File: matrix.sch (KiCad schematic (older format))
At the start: 133 parts

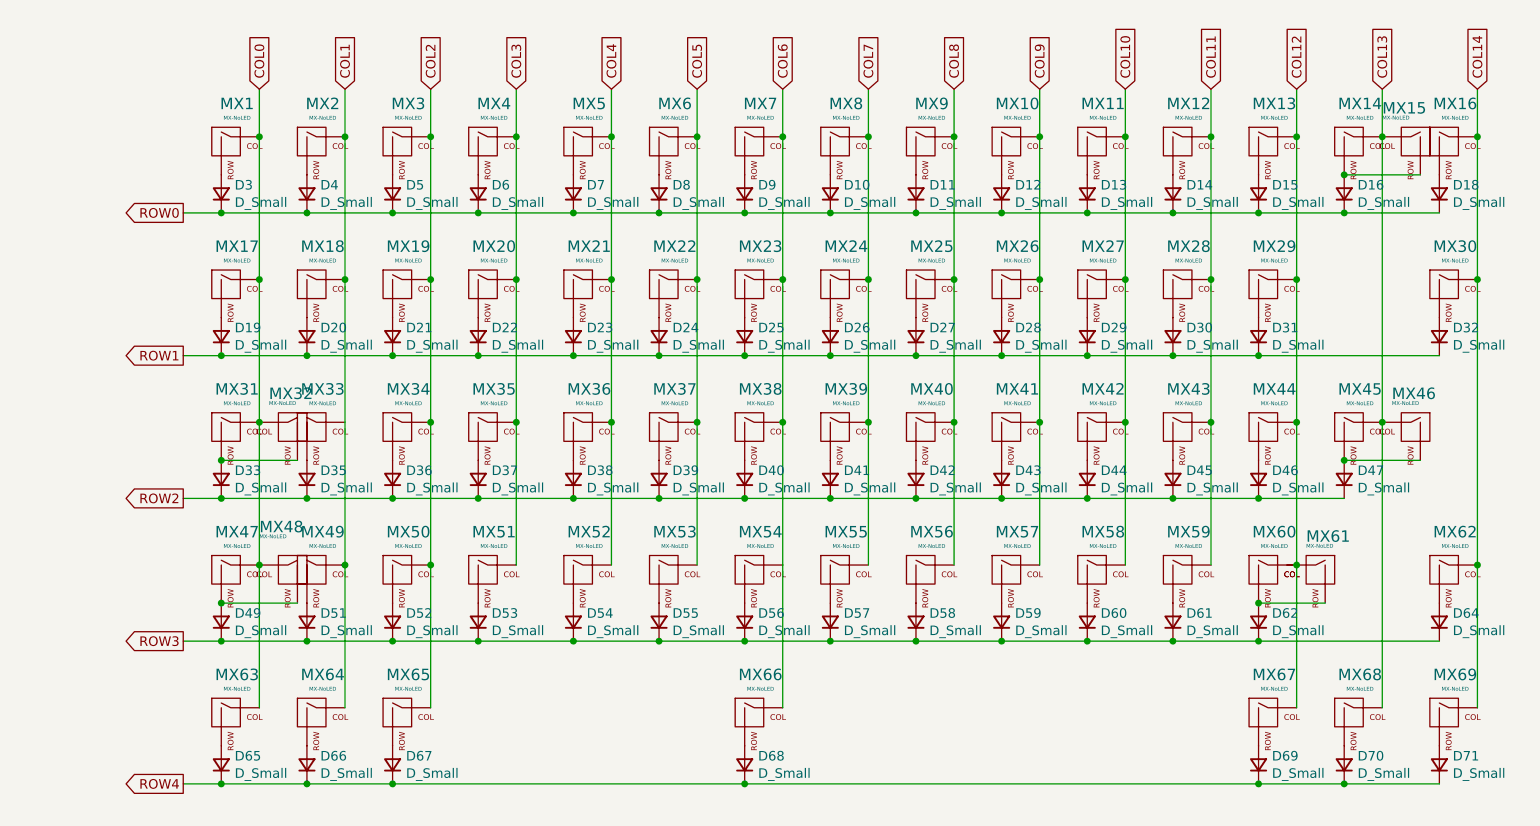
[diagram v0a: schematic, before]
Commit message: fixed schematic flaws and caps lock (thanks Martin!)
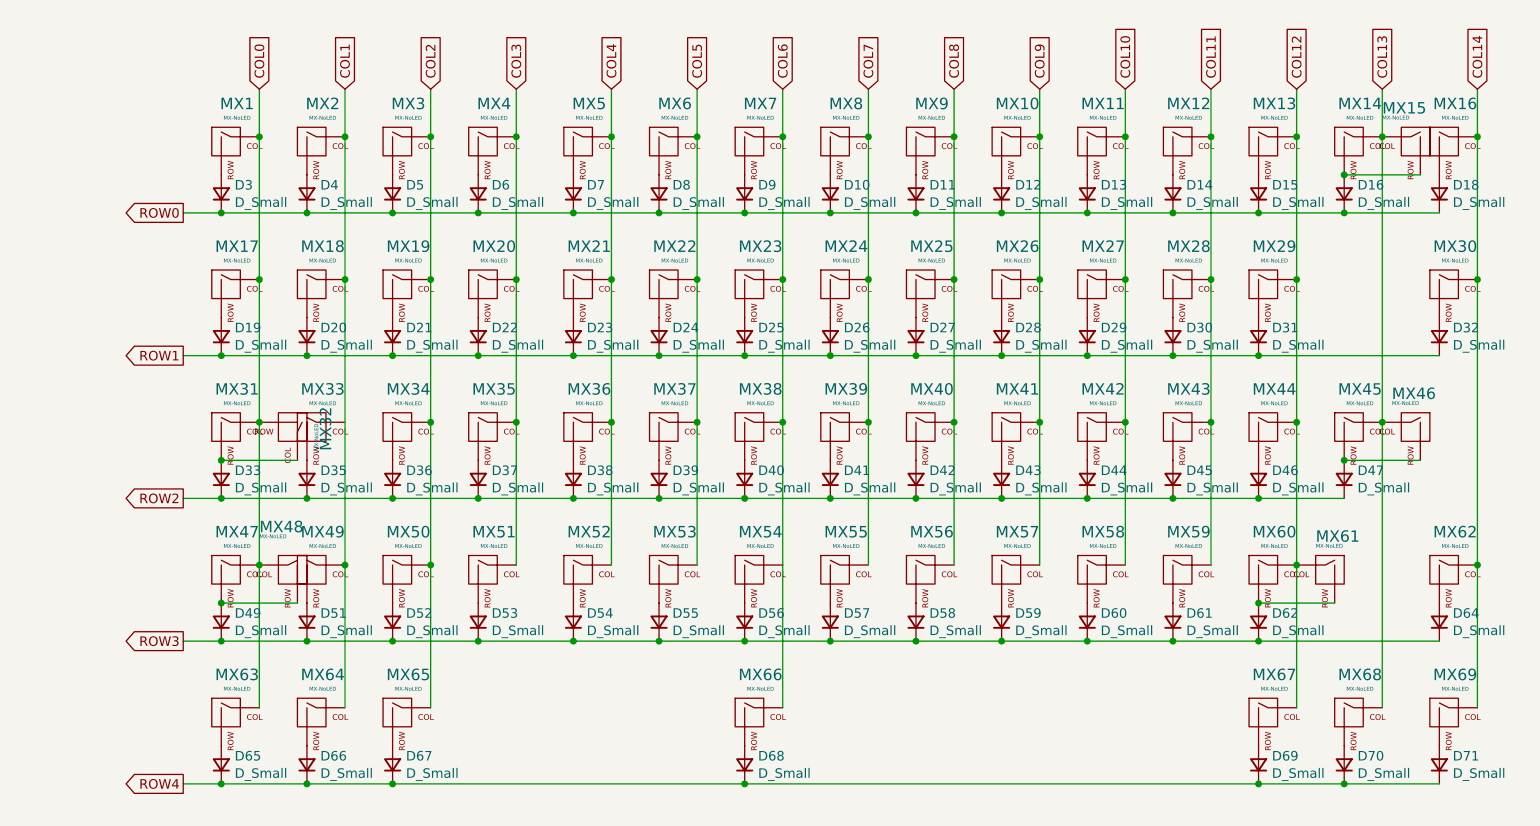
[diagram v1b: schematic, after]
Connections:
- net COL0: now also MX32.2 (ROW); no longer MX32.1 (COL)
- net COL12: now also MX61.1 (COL)
- net at D33.2 (A), MX31.2 (ROW): now also MX32.1 (COL); no longer MX32.2 (ROW)
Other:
- moved on the sheet: MX61
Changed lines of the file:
@@
 	7300 2100 7300 2850
 Connection ~ 7300 2100
-Wire Wire Line
-	7300 3600 7300 4350
 $Comp
 L MX_Alps_Hybrid:MX-NoLED MX16
@@
 Connection ~ 7300 3600
 Connection ~ 7300 2850
-$Comp
-L MX_Alps_Hybrid:MX-NoLED MX61
-U 1 1 61165F70
-P 7400 3650
-F 0 "MX61" H 7450 3850 60  0000 R CNN
-F 1 "MX-NoLED" H 7450 3800 20  0000 R CNN
-F 2 "MX_Only:MXOnly-2.75U-NoLED" H 6775 3625 60  0001 C CNN
-F 3 "" H 6775 3625 60  0001 C CNN
-	1    7400 3650
-	-1   0    0    -1
-$EndComp
 Connection ~ 7100 4000
 $Comp
@@
 F 3 "" H 1375 2875 60  0001 C CNN
 	1    2000 2900
-	-1   0    0    -1
+	0    1    1    0
 $EndComp
 Wire Wire Line
@@
 	2050 3800 1650 3800
 Connection ~ 1650 3800
-Wire Wire Line
-	2050 3050 1650 3050
 Connection ~ 1650 3050
 Wire Wire Line
@@
 Wire Wire Line
 	7100 4000 8050 4000
-Wire Wire Line
-	7450 3800 7100 3800
 Connection ~ 7100 3800
 Wire Wire Line
@@
 Connection ~ 2100 3250
 Connection ~ 1650 3250
+Wire Wire Line
+	7300 3600 7300 4350
+$Comp
+L MX_Alps_Hybrid:MX-NoLED MX61
+U 1 1 61165F70
+P 7450 3650
+F 0 "MX61" H 7500 3850 60  0000 R CNN
+F 1 "MX-NoLED" H 7500 3800 20  0000 R CNN
+F 2 "MX_Only:MXOnly-2.75U-NoLED" H 6825 3625 60  0001 C CNN
+F 3 "" H 6825 3625 60  0001 C CNN
+	1    7450 3650
+	-1   0    0    -1
+$EndComp
+Wire Wire Line
+	7100 3800 7500 3800
+Wire Wire Line
+	1650 3050 2050 3050
 $EndSCHEMATC

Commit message: minor fixes
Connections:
- net COL1: now also MX33.1 (COL)
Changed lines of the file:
@@
 	-1   0    0    -1
 $EndComp
-Wire Wire Line
-	2300 3600 2300 2100
-Connection ~ 2300 3600
 Connection ~ 2300 1350
 Wire Wire Line
@@
 	2750 1350 2750 2100
 Connection ~ 2100 2500
-Connection ~ 2300 2100
 Wire Wire Line
 	2300 2100 2300 1350
@@
 Wire Wire Line
 	1650 3050 2050 3050
+Wire Wire Line
+	2300 3600 2300 2850
+Connection ~ 2300 3600
+Wire Wire Line
+	2300 2850 2300 2100
+Connection ~ 2300 2850
+Connection ~ 2300 2100
 $EndSCHEMATC

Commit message: updated branch and ordered pcb prototype
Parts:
- D10, D11, D12, D13, D14, D15, D16, D18, D19, D20, D21, D22, D23, D24, D25, D26, D27, D28, D29, D3, D30, D31, D32, D33, D35, D36, D37, D38, D39, D4, D40, D41, D42, D43, D44, D45, D46, D47, D49, D5, D51, D52, D53, D54, D55, D56, D57, D58, D59, D6, D60, D61, D62, D64, D65, D66, D67, D68, D69, D7, D70, D71, D8, D9: value D_Small -> 1n4148; footprint Diode_SMD:D_0603_1608Metric -> Diode_SMD:D_SOD-323F; JLCPCB (none) -> C2128

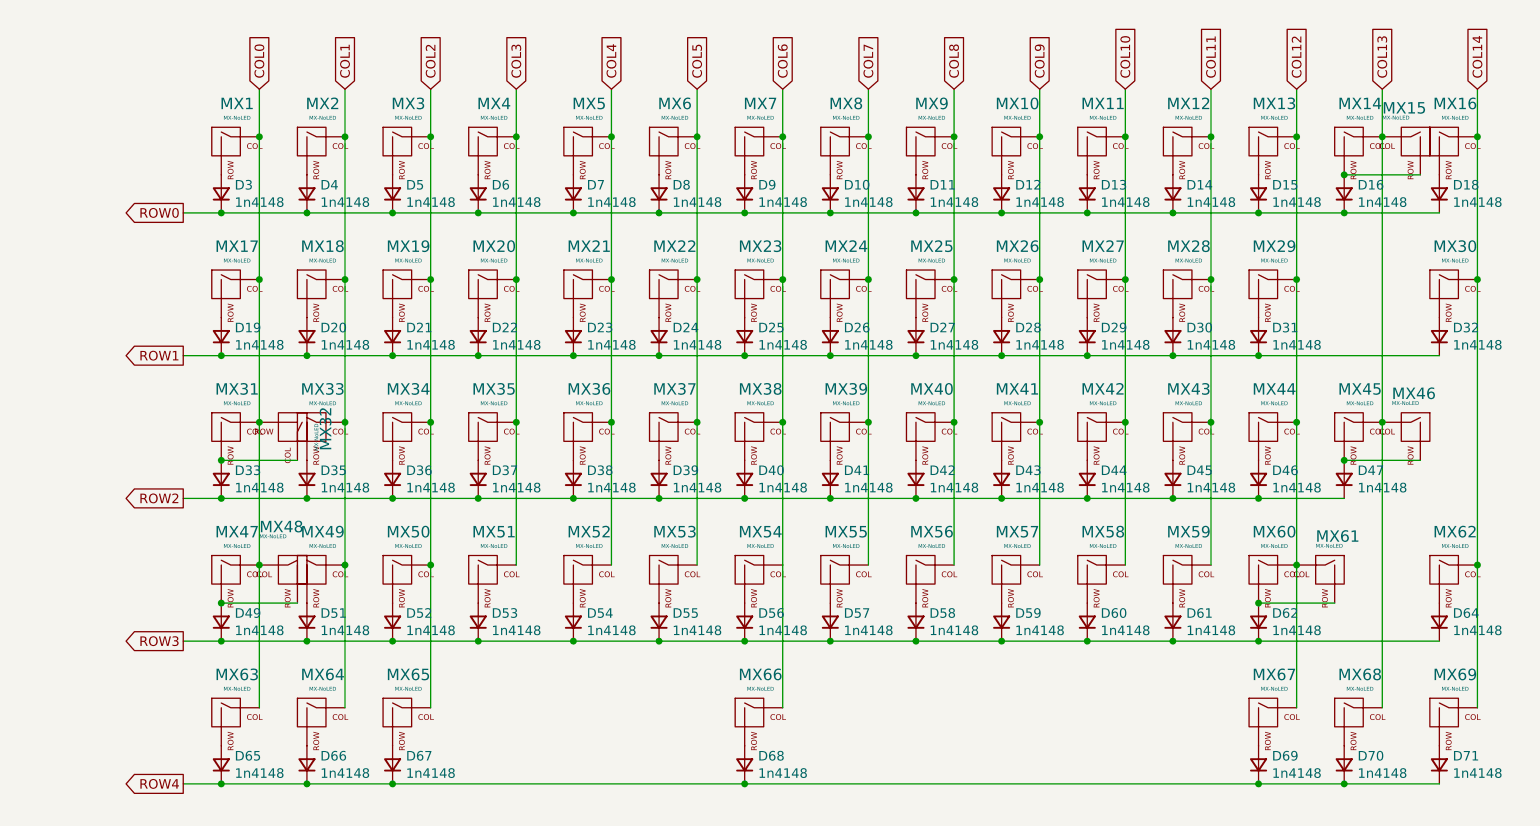
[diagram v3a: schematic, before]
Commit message: modified to use BAV70 diodes
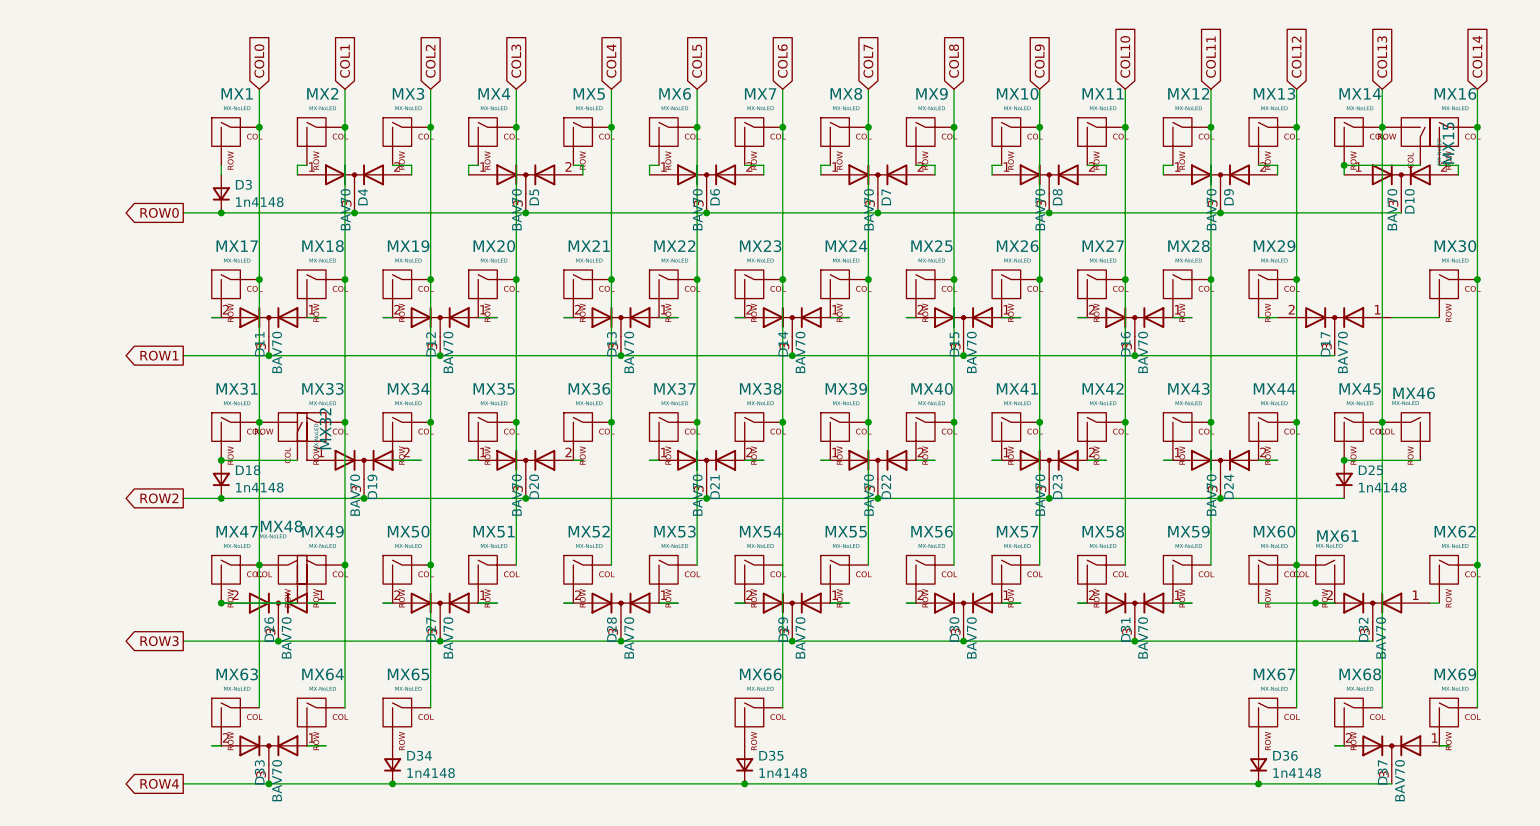
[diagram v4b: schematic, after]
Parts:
- removed D10, D11, D12, D13, D14, D15, D16, D18, D19, D20, D21, D22, D23, D24, D25, D26, D27, D28, D29, D30, D31, D32, D35, D36, D37, D38, D39, D4, D40, D41, D42, D43, D44, D45, D46, D49, D5, D51, D52, D53, D54, D55, D56, D57, D58, D59, D6, D60, D61, D62, D64, D65, D66, D7, D70, D71, D8, D9: 1n4148, Diode_SMD:D_SOD-323F, symbol Device:D_Small
- added D10, D11, D12, D13, D14, D15, D16, D17, D19, D20, D21, D22, D23, D24, D26, D27, D28, D29, D30, D31, D32, D33, D37, D4, D5, D6, D7, D8, D9: BAV70, Package_TO_SOT_SMD:SOT-23, symbol Diode:BAV70
- renumbered D33 to D18, D47 to D25, D67 to D34, D68 to D35, D69 to D36
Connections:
- net COL13: now also MX15.2 (ROW); no longer MX15.1 (COL)
- net ROW0: now also D10.3 (K), D4.3 (K), D5.3 (K), D6.3 (K), D7.3 (K), D8.3 (K), D9.3 (K)
- net ROW1: now also D11.3 (K), D12.3 (K), D13.3 (K), D14.3 (K), D15.3 (K), D16.3 (K), D17.3 (K)
- net ROW2: now also D19.3 (K), D20.3 (K), D21.3 (K), D22.3 (K), D23.3 (K), D24.3 (K)
- net ROW3: now also D26.3 (K), D27.3 (K), D28.3 (K), D29.3 (K), D30.3 (K), D31.3 (K), D32.3 (K)
- net ROW4: now also D33.3 (K), D37.3 (K)
- net at MX2.2 (ROW): now also D4.1 (A)
- net at MX17.2 (ROW): now also D11.2 (A)
- net at MX47.2 (ROW), MX48.2 (ROW): now also D26.2 (A)
- net at MX49.2 (ROW): now also D26.1 (A)
- net at MX63.2 (ROW): now also D33.2 (A)
- net at MX64.2 (ROW): now also D33.1 (A)
- net at MX3.2 (ROW): now also D4.2 (A)
- net at MX4.2 (ROW): now also D5.1 (A)
- net at MX18.2 (ROW): now also D11.1 (A)
- net at MX19.2 (ROW): now also D12.2 (A)
- net at MX34.2 (ROW): now also D19.2 (A)
- net at MX35.2 (ROW): now also D20.1 (A)
- net at MX50.2 (ROW): now also D27.2 (A)
- net at MX51.2 (ROW): now also D27.1 (A)
- net at MX5.2 (ROW): now also D5.2 (A)
- net at MX6.2 (ROW): now also D6.1 (A)
- net at MX21.2 (ROW): now also D13.2 (A)
- net at MX22.2 (ROW): now also D13.1 (A)
- net at MX36.2 (ROW): now also D20.2 (A)
- net at MX37.2 (ROW): now also D21.1 (A)
- net at MX52.2 (ROW): now also D28.2 (A)
- net at MX53.2 (ROW): now also D28.1 (A)
- net at MX7.2 (ROW): now also D6.2 (A)
- net at MX8.2 (ROW): now also D7.1 (A)
- net at MX23.2 (ROW): now also D14.2 (A)
- net at MX24.2 (ROW): now also D14.1 (A)
- net at MX38.2 (ROW): now also D21.2 (A)
- net at MX39.2 (ROW): now also D22.1 (A)
- net at MX54.2 (ROW): now also D29.2 (A)
- net at MX55.2 (ROW): now also D29.1 (A)
- net at MX9.2 (ROW): now also D7.2 (A)
- net at MX10.2 (ROW): now also D8.1 (A)
- net at MX25.2 (ROW): now also D15.2 (A)
- net at MX26.2 (ROW): now also D15.1 (A)
- net at MX40.2 (ROW): now also D22.2 (A)
- net at MX41.2 (ROW): now also D23.1 (A)
- net at MX56.2 (ROW): now also D30.2 (A)
- net at MX57.2 (ROW): now also D30.1 (A)
- net at MX11.2 (ROW): now also D8.2 (A)
- net at MX12.2 (ROW): now also D9.1 (A)
- net at MX27.2 (ROW): now also D16.2 (A)
- net at MX28.2 (ROW): now also D16.1 (A)
- net at MX42.2 (ROW): now also D23.2 (A)
- net at MX43.2 (ROW): now also D24.1 (A)
- net at MX58.2 (ROW): now also D31.2 (A)
- net at MX59.2 (ROW): now also D31.1 (A)
- net at MX13.2 (ROW): now also D9.2 (A)
- net at MX14.2 (ROW): now also MX15.1 (COL), D10.1 (A); no longer MX15.2 (ROW)
- net at MX29.2 (ROW): now also D17.2 (A)
- net at MX44.2 (ROW): now also D24.2 (A)
- net at MX60.2 (ROW), MX61.2 (ROW): now also D32.2 (A)
- net at MX16.2 (ROW): now also D10.2 (A)
- net at MX62.2 (ROW): now also D32.1 (A)
- net at MX33.2 (ROW): now also D19.1 (A)
- net at MX20.2 (ROW): now also D12.1 (A)
- net at MX69.2 (ROW): now also D37.1 (A)
- net at MX68.2 (ROW): now also D37.2 (A)
- net at MX30.2 (ROW): now also D17.1 (A)
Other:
- moved on the sheet: MX1, MX10, MX11, MX12, MX13, MX14, MX15, MX16, MX2, MX3, MX4, MX5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
